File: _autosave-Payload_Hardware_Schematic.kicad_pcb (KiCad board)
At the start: 2 copper layers, 118 x 56 mm, 14 parts, among them J1 Micro_SD_Card, J3 Conn_01x04_Pin, J4 Conn_01x02, J5 Conn_01x04_Pin, J6 Conn_01x04_Socket, U1 STM32F411 BlackPill, U2 MPM3610, U4 LSM9DS1, U5 MPM3610, U6 BMP388

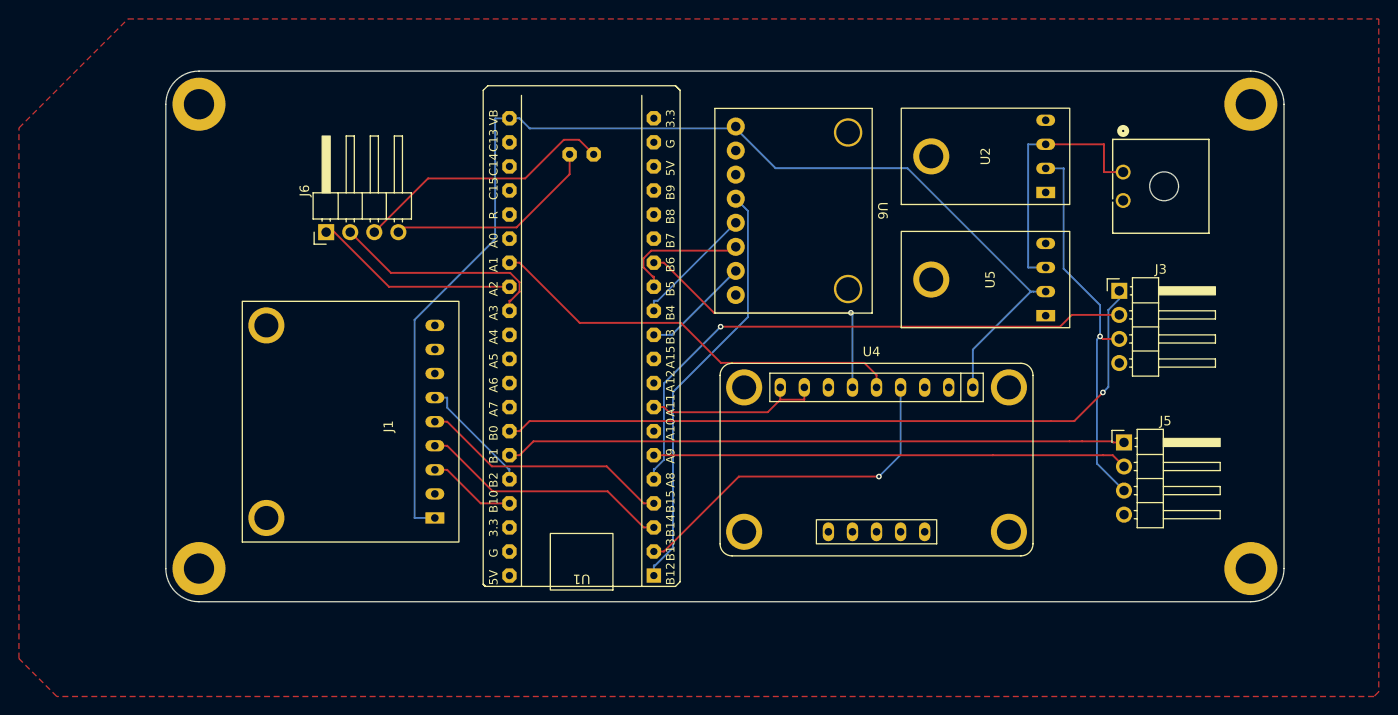
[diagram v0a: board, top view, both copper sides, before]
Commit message: finalized board, changed Vbat to 3.3V
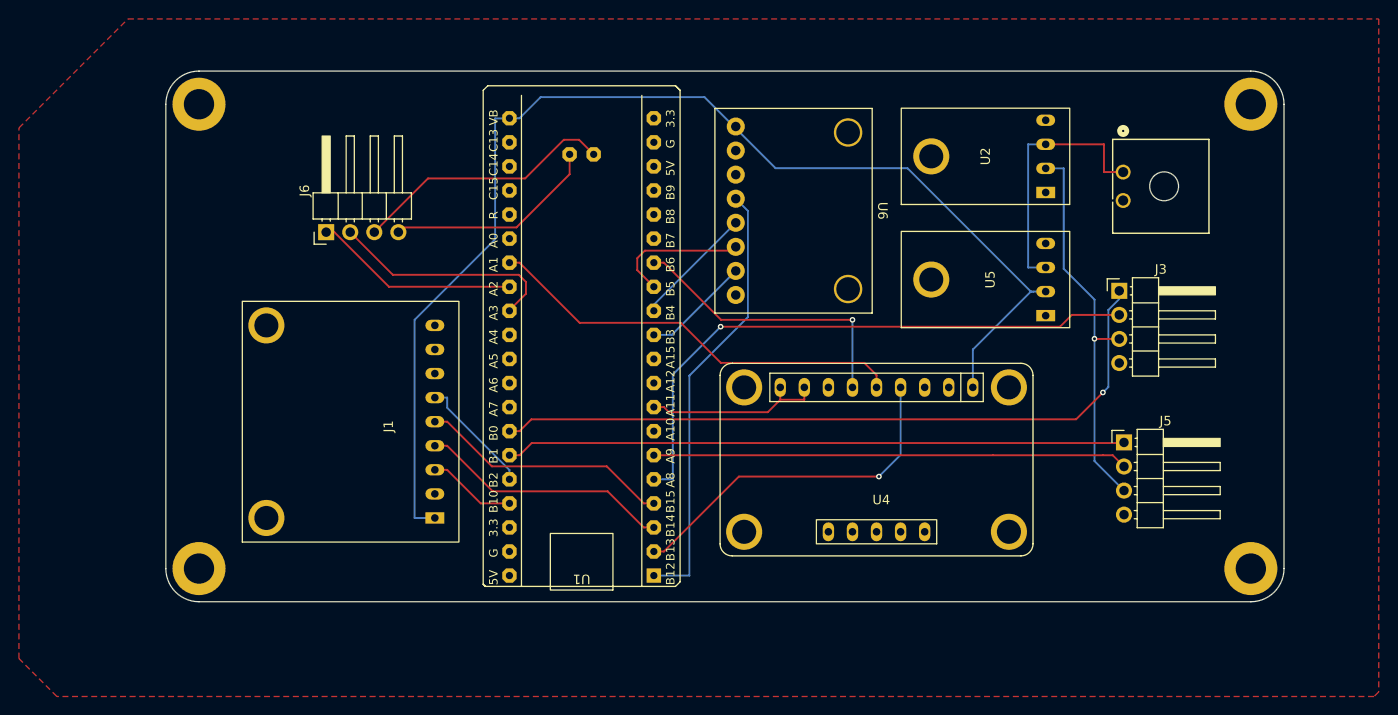
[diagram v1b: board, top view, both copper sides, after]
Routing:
- net /SCK3: track 44.5 -> 46.6 mm
- net /<NO NET>: track 126.4 -> 128.2 mm
- net /TIM1: track 61.7 -> 62.8 mm
- net /UART_RX: track 23.6 -> 24.5 mm
- net /MOSI3: track 13.8 -> 14.6 mm

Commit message: Switched sd card and uart/serial access
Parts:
- moved J6 22.1 mm to (91.8, 78.6), turned to -90 degrees
- moved J1 17.0 mm to (96.4, 60.5)
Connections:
- U1 pad 20: unconnected-(U1-3.3V-Pad20) -> /<NO NET>
- U1 pad 21: /<NO NET> -> unconnected-(U1-VBat-Pad21)
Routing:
- net /SCK: track 22.7 -> 48.3 mm, vias 0 -> 1
- net /DIO: track 27.8 -> 52.4 mm, vias 0 -> 1
- net /<NO NET>: track 128.2 -> 106.9 mm, vias 0 -> 1
- net /MOSI2: track 26.7 -> 44.1 mm, vias 0 -> 1
- net /NSS2: track 12.6 -> 29.8 mm
- net /SCK2: track 9.34 -> 25.2 mm
- net /MISO2: track 26.7 -> 42.2 mm, vias 0 -> 1
- net /UART_TX: track 21.7 -> 35.3 mm
- net /UART_RX: track 24.5 -> 26.1 mm, vias 0 -> 1

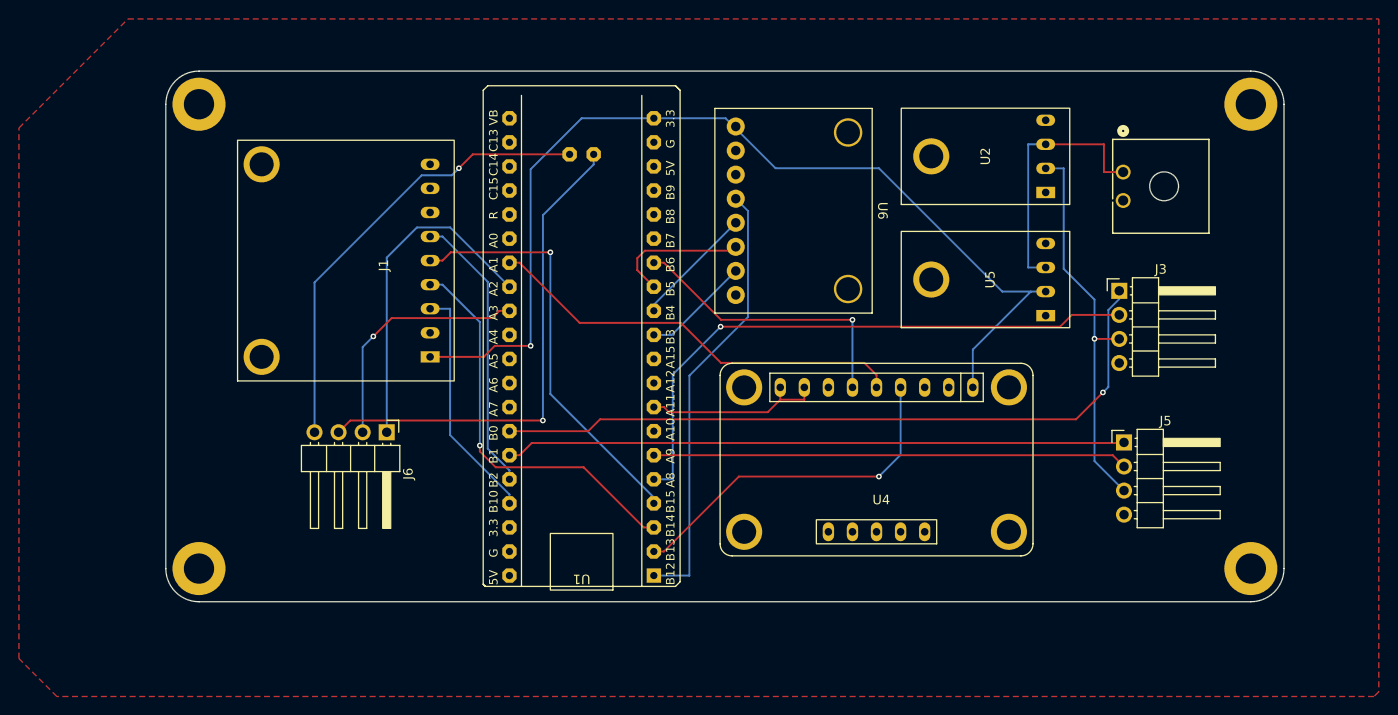
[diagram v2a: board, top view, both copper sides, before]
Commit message: Niv's edits, moved pins close to edge and connected servos to 7.2V
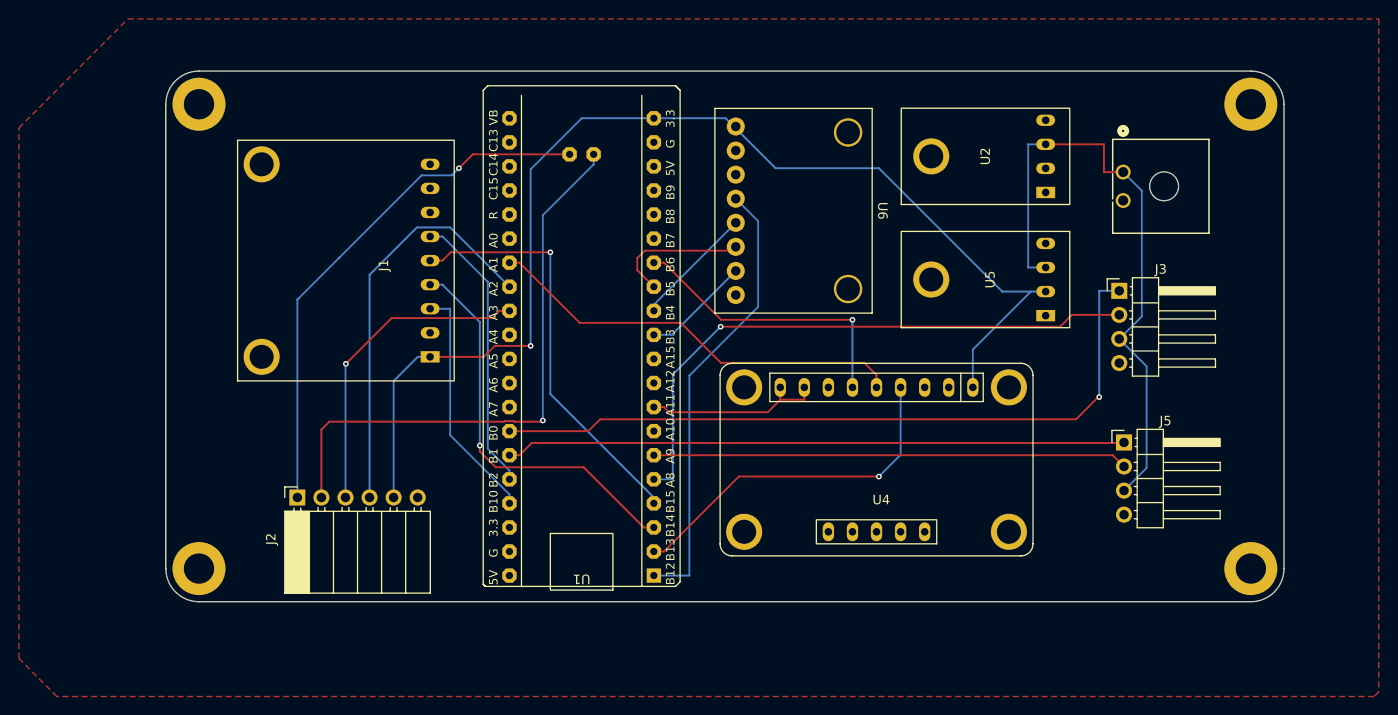
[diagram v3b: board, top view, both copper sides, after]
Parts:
- removed J6: Conn_01x04_Socket, Connector_PinHeader_2.54mm:PinHeader_1x04_P2.54mm_Horizontal
- added J2: Conn_01x06_Socket, Connector_PinSocket_2.54mm:PinSocket_1x06_P2.54mm_Horizontal, F.Cu at (82.4, 85.5)
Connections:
- J3 pad 3: /5V -> /7.2V
- J5 pad 3: /5V -> /7.2V
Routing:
- net /5V: track 41.2 -> 0.00 mm, vias 1 -> 0
- net /7.2V: track 27.8 -> 65.4 mm
- net /<NO NET>: track 106.9 -> 124.1 mm
- net /DIO: track 52.4 -> 61.8 mm
- net /SCK: track 48.3 -> 56.7 mm
- net /UART_RX: track 26.1 -> 34.2 mm
- net /UART_TX: track 35.3 -> 43.5 mm
- net /FDBK1: track 75.8 -> 77.1 mm
- net /SCK3: track 46.6 -> 47.5 mm
